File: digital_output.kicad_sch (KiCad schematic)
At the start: 12 parts, among them Q1 AOSP21321, Q2 AOSP21321, Q3 NMOS, Q4 NMOS

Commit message: more routing
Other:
- moved on the sheet: Q4
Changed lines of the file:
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@@
+	)
+	(junction
+		(at 72.39 67.31)
+		(diameter 0)
+		(color 0 0 0 0)
 	)
 	(junction
@@
 		(color 0 0 0 0)
 	)
-	(junction
-		(at 71.12 67.31)
-		(diameter 0)
-		(color 0 0 0 0)
-	)
 	(wire
 		(pts
@@
 	(wire
 		(pts
+			(xy 63.5 88.9) (xy 62.23 88.9)
+		)
+		(stroke
+			(width 0)
+			(type default)
+		)
+	)
+	(wire
+		(pts
 			(xy 36.83 58.42) (xy 36.83 57.15)
 		)
@@
 	(wire
 		(pts
+			(xy 72.39 67.31) (xy 71.12 67.31)
+		)
+		(stroke
+			(width 0)
+			(type default)
+		)
+	)
+	(wire
+		(pts
+			(xy 63.5 91.44) (xy 63.5 88.9)
+		)
+		(stroke
+			(width 0)
+			(type default)
+		)
+	)
+	(wire
+		(pts
 			(xy 19.05 83.82) (xy 19.05 88.9)
 		)
@@
 	(wire
 		(pts
-			(xy 71.12 67.31) (xy 71.12 83.82)
+			(xy 72.39 67.31) (xy 72.39 86.36)
 		)
 		(stroke
@@
 	(wire
 		(pts
+			(xy 71.12 95.25) (xy 71.12 99.06)
+		)
+		(stroke
+			(width 0)
+			(type default)
+		)
+	)
+	(wire
+		(pts
 			(xy 53.34 83.82) (xy 53.34 88.9)
 		)
@@
 	(wire
 		(pts
-			(xy 71.12 93.98) (xy 71.12 99.06)
+			(xy 72.39 96.52) (xy 72.39 95.25)
 		)
 		(stroke
@@
 	(wire
 		(pts
-			(xy 71.12 67.31) (xy 72.39 67.31)
-		)
-		(stroke
-			(width 0)
-			(type default)
-		)
-	)
-	(wire
-		(pts
 			(xy 53.34 90.17) (xy 53.34 88.9)
 		)
@@
 	(wire
 		(pts
-			(xy 62.23 88.9) (xy 63.5 88.9)
+			(xy 63.5 91.44) (xy 64.77 91.44)
 		)
 		(stroke
@@
 		(pts
 			(xy 27.94 88.9) (xy 29.21 88.9)
+		)
+		(stroke
+			(width 0)
+			(type default)
+		)
+	)
+	(wire
+		(pts
+			(xy 72.39 95.25) (xy 71.12 95.25)
 		)
 		(stroke
@@
 	(symbol
 		(lib_id "Simulation_SPICE:NMOS")
-		(at 68.58 88.9 0)
+		(at 69.85 91.44 0)
 		(unit 1)
 		(exclude_from_sim no)
@@
 		(dnp no)
 		(property "Reference" "Q4"
-			(at 63.5 91.44 0)
+			(at 64.77 93.98 0)
 			(effects
 				(font
@@
 		)
 		(property "Value" "NMOS"
-			(at 63.5 93.98 0)
+			(at 64.77 96.52 0)
 			(effects
 				(font
@@
 		)
 		(property "Footprint" "Package_TO_SOT_SMD:SOT-23"
-			(at 73.66 86.36 0)
+			(at 74.93 88.9 0)
 			(effects
 				(font
@@
 		)
 		(property "Datasheet" "https://ngspice.sourceforge.io/docs/ngspice-manual.pdf"
-			(at 68.58 101.6 0)
+			(at 69.85 104.14 0)
 			(effects
 				(font
@@
 		)
 		(property "Description" ""
-			(at 68.58 88.9 0)
+			(at 69.85 91.44 0)
 			(effects
 				(font
@@
 		)
 		(property "Sim.Device" "NMOS"
-			(at 68.58 106.045 0)
+			(at 69.85 108.585 0)
 			(effects
 				(font
@@
 		)
 		(property "Sim.Type" "VDMOS"
-			(at 68.58 107.95 0)
+			(at 69.85 110.49 0)
 			(effects
 				(font
@@
 		)
 		(property "Sim.Pins" "1=D 2=G 3=S"
-			(at 68.58 104.14 0)
+			(at 69.85 106.68 0)
 			(effects
 				(font
@@
 		)
 		(property "LCSC#" "C20917"
-			(at 68.58 88.9 0)
+			(at 69.85 91.44 0)
 			(effects
 				(font
@@
 		)
 		(property "Manufacturer" "Alpha & Omega Semicon"
-			(at 68.58 88.9 0)
+			(at 69.85 91.44 0)
 			(effects
 				(font
@@
 		)
 		(property "Part#" "AO3400A"
-			(at 68.58 88.9 0)
-			(effects
-				(font
+			(at 69.85 91.44 0)
+			(effects
+				(font

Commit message: added comment for mosfet todo
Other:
- note added: "@TODO: fix mosfet rotation issue!!!"
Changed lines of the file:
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@@
+		)
+	)
+	(text "@TODO:\nfix mosfet rotation issue!!!"
+		(exclude_from_sim no)
+		(at 40.64 109.22 0)
+		(effects
+			(font
+				(size 1.27 1.27)
+			)
+			(justify left)
 		)
 	)

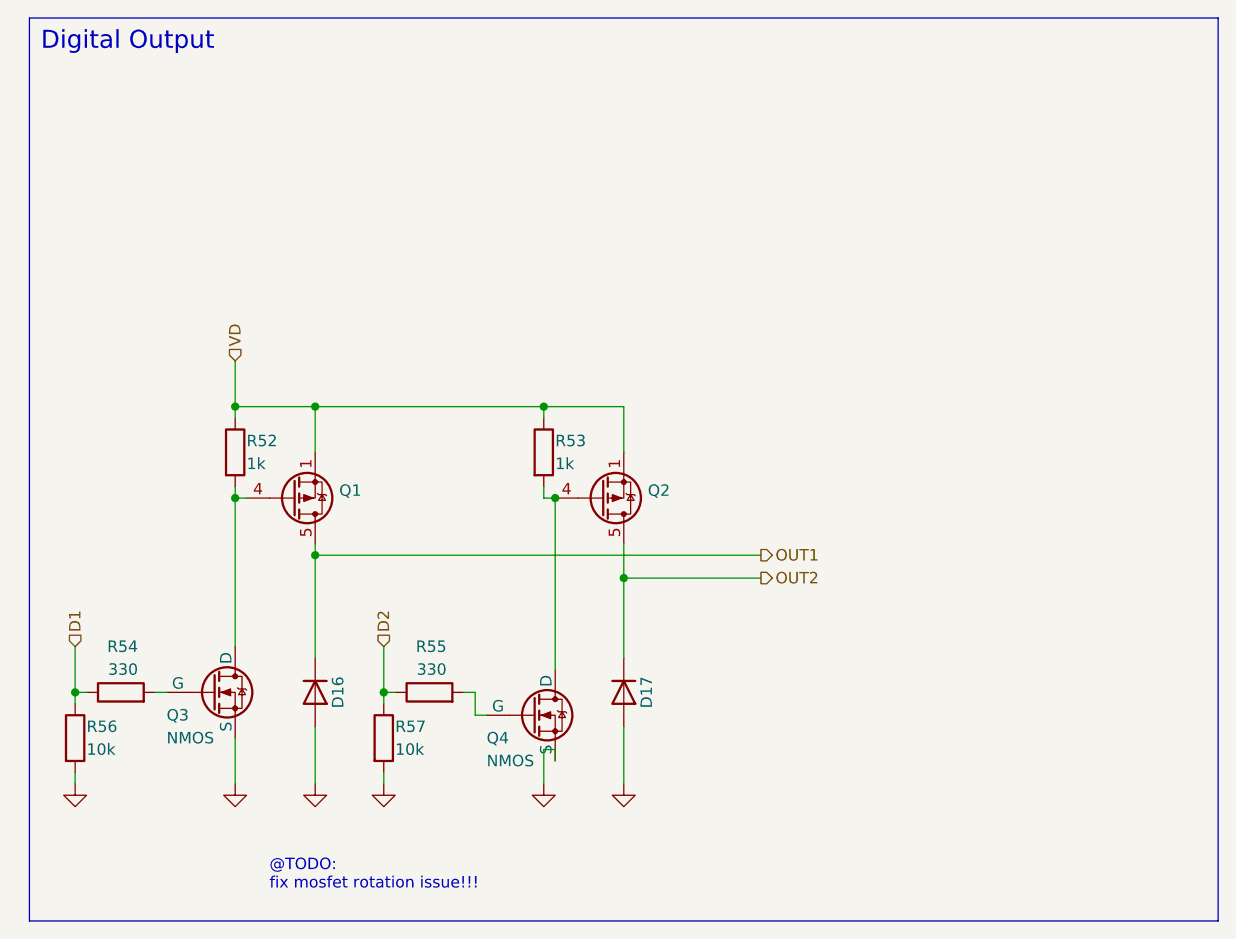
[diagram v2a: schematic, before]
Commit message: fixed transistor rotation issue, filter vs farrite bead, 5V supply for servos, and others in scematic
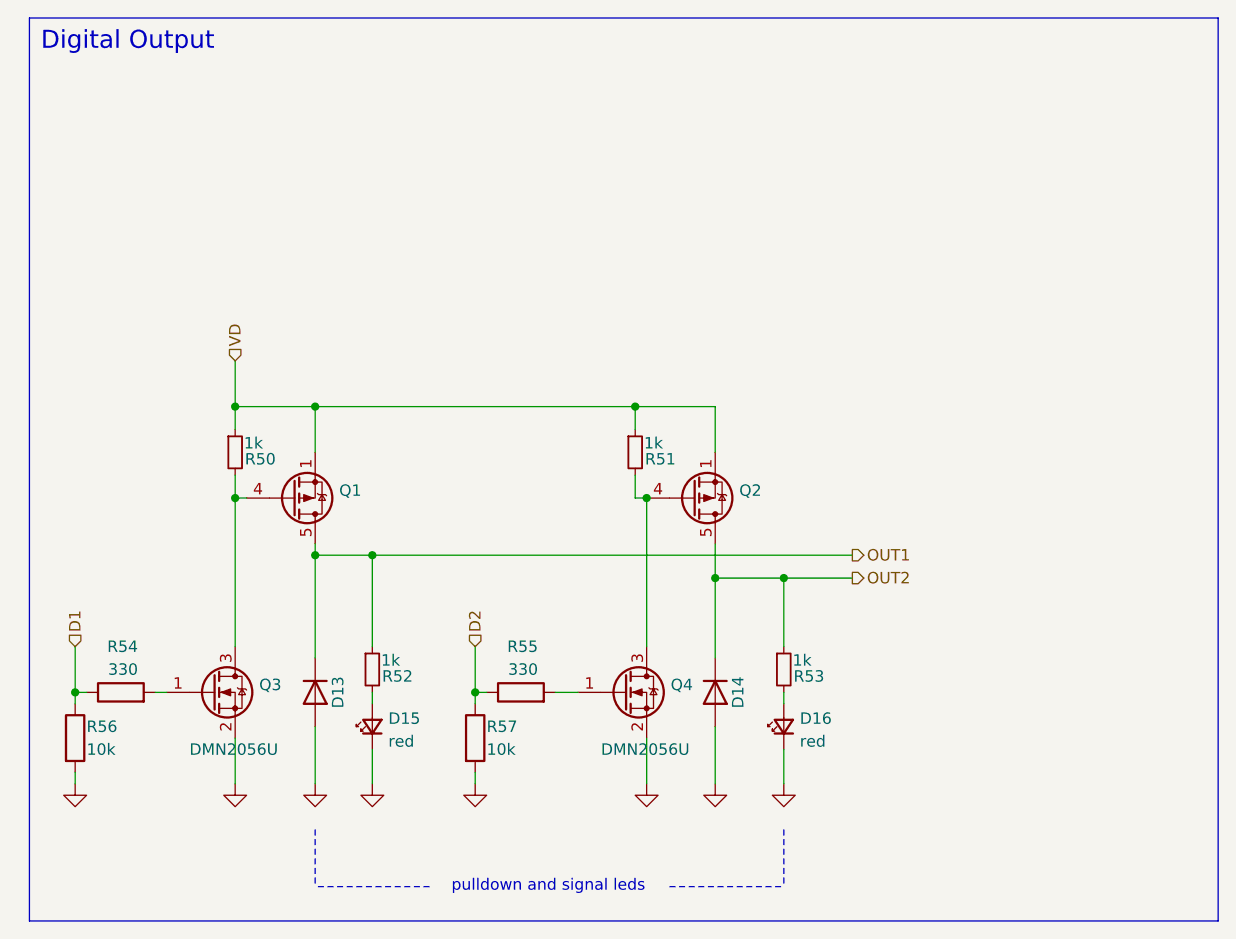
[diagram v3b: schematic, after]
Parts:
- removed Q3, Q4: NMOS, Package_TO_SOT_SMD:SOT-23, symbol Simulation_SPICE:NMOS
- removed R52, R53: 1k, Resistor_SMD:R_0603_1608Metric_Pad0.98x0.95mm_HandSolder, symbol Device:R
- added D15, D16: red, LED_SMD:LED_0603_1608Metric, symbol Device:LED_Small
- added Q3, Q4: DMN2056U, Package_TO_SOT_SMD:SOT-23, symbol Transistor_FET:DMG2302U
- added R50, R51, R52, R53: 1k, Resistor_SMD:R_0402_1005Metric, symbol Device:R_Small
- renumbered D16 to D13, D17 to D14
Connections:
- net GND: now also D15.1 (K), D16.1 (K), Q3.2 (S), Q4.2 (S)
- net OUT1: now also R52.1
- net OUT2: now also R53.1
- net VD: now also R50.1, R51.1
- net at Q1.4 (G): now also Q3.3 (D), R50.2
- net at Q2.4 (G): now also Q4.3 (D), R51.2
- net at R55.2: now also Q4.1 (G)
- net at R54.2: now also Q3.1 (G)
- new net: D15.2 (A), R52.2
- new net: D16.2 (A), R53.2
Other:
- note added: "pulldown and signal leds"
- note removed: "@TODO: fix mosfet rotation issue!!!"
- moved on the sheet: D14, Q2, R55, R57

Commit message: started routing
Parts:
- D13, D14: footprint Diode_SMD:D_SOD-323_HandSoldering -> Diode_SMD:D_SOD-123F; LCSC (none) -> C64898; LCSC# C7528872 -> (none)
- D15, D16: LCSC (none) -> C965799; LCSC# C965799 -> (none)
- Q1, Q2: footprint Package_SO:SO-8_3.9x4.9mm_P1.27mm -> Package_SO:SOIC-8_3.9x4.9mm_P1.27mm; LCSC (none) -> C560863; LCSC# C560863 -> (none)
- R52: renamed from R50; LCSC (none) -> C11702; LCSC# C2906899 -> (none); Manufacturer FOJAN -> (none); Part# FRC0402J102 TS -> (none)
- R53: renamed from R51; LCSC (none) -> C11702; LCSC# C2906899 -> (none); Manufacturer FOJAN -> (none); Part# FRC0402J102 TS -> (none)
- R54: renamed from R52; LCSC (none) -> C11702; LCSC# C2906899 -> (none); Manufacturer FOJAN -> (none); Part# FRC0402J102 TS -> (none)
- R55: renamed from R53; LCSC (none) -> C11702; LCSC# C2906899 -> (none); Manufacturer FOJAN -> (none); Part# FRC0402J102 TS -> (none)
- R56: renamed from R54; footprint Resistor_SMD:R_0603_1608Metric_Pad0.98x0.95mm_HandSolder -> Resistor_SMD:R_0402_1005Metric; LCSC (none) -> C25104; LCSC# C23138 -> (none)
- R57: renamed from R55; footprint Resistor_SMD:R_0603_1608Metric_Pad0.98x0.95mm_HandSolder -> Resistor_SMD:R_0402_1005Metric; LCSC (none) -> C25104; LCSC# C23138 -> (none)
- R58: renamed from R56; footprint Resistor_SMD:R_0603_1608Metric_Pad0.98x0.95mm_HandSolder -> Resistor_SMD:R_0402_1005Metric; LCSC (none) -> C25744; LCSC# C25804 -> (none)
- R59: renamed from R57; footprint Resistor_SMD:R_0603_1608Metric_Pad0.98x0.95mm_HandSolder -> Resistor_SMD:R_0402_1005Metric; LCSC (none) -> C25744; LCSC# C25804 -> (none)
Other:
- note added: "use 0402!!"
- moved on the sheet: D13, D14, D15, D16, Q1, Q2, Q3, Q4, R52, R53, R54, R55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

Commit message: finished routing
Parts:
- added R32, R73: 10k, Resistor_SMD:R_0402_1005Metric, symbol Device:R
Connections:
- net GND: now also R32.2, R73.2
- net OUT1: now also R32.1
- net OUT2: now also R73.1
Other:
- note removed: "use 0402!!"
- moved on the sheet: D14, D16, Q2, Q4, R53, R55, R57, R59

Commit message: started silkscrean
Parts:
- renumbered D14 to D10, D15 to D11, D16 to D12, D13 to D9, R52 to R49, R53 to R50, R54 to R51, R55 to R52, R32 to R53, R73 to R54, R56 to R55, R57 to R56, R58 to R57, R59 to R58

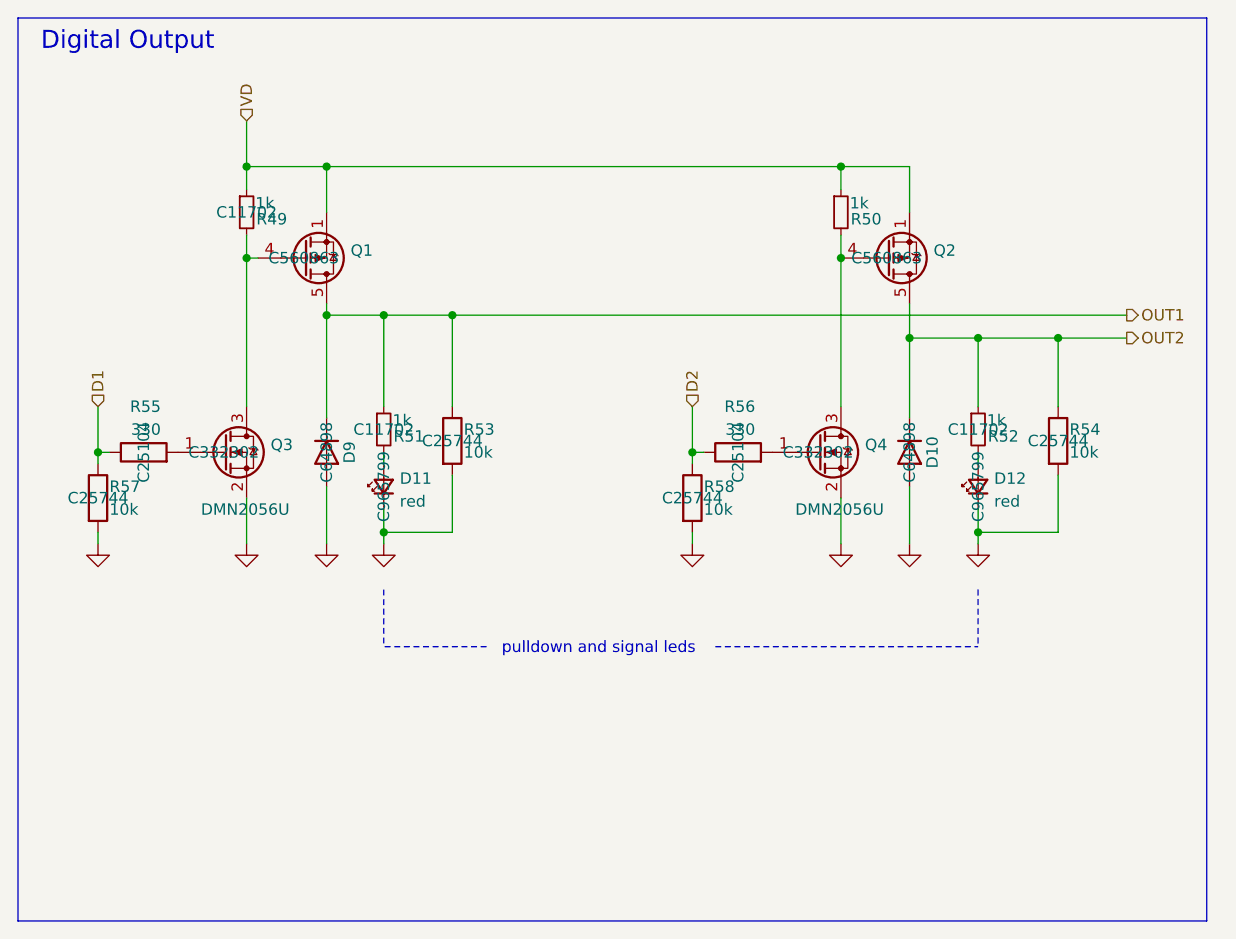
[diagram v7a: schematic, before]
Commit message: high current inputs: change pmos pullup and led resistors
Apparently Kicad also saved files in a new format.
I was using Kicad version 10.0
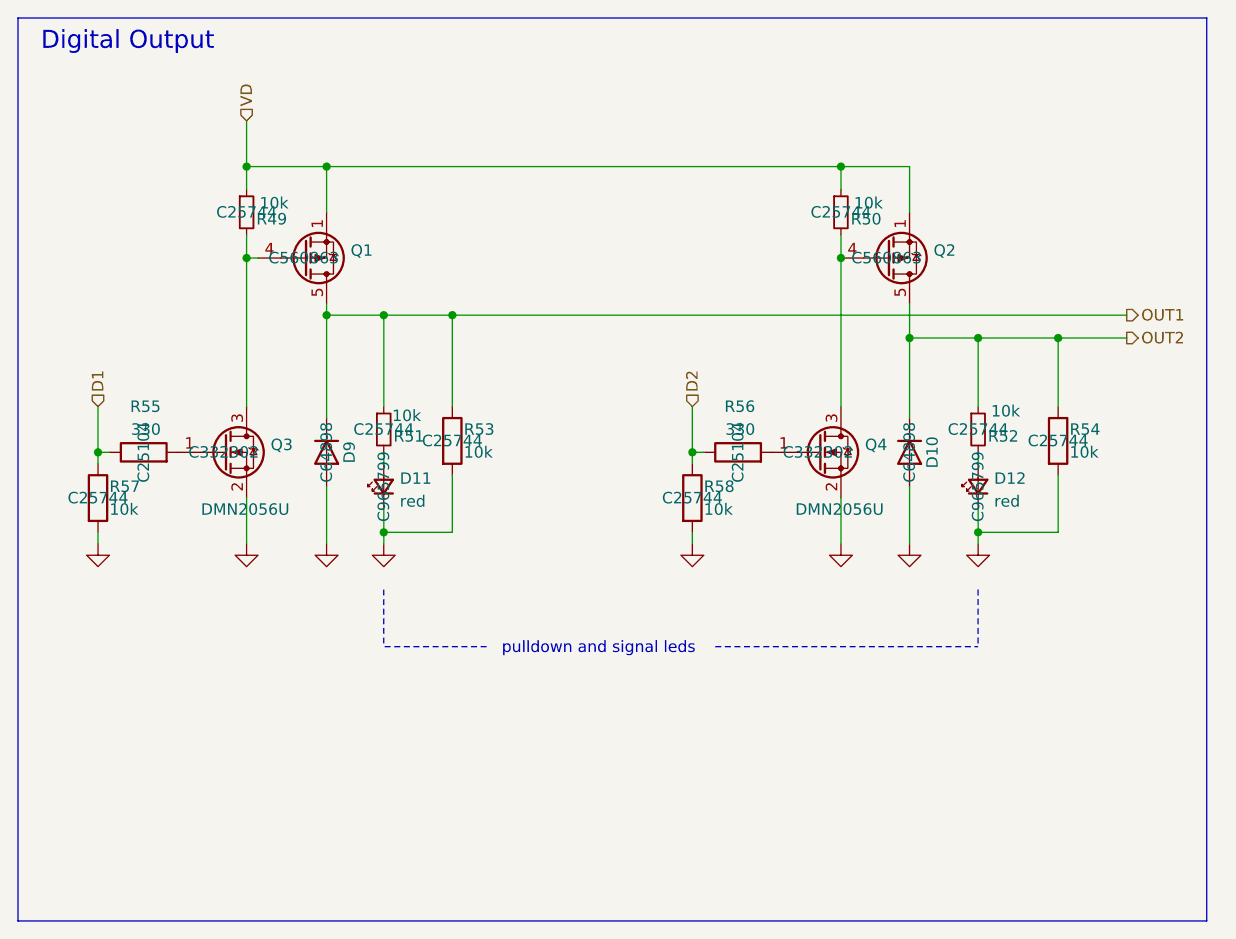
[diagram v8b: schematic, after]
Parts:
- R49, R50, R51, R52: value 1k -> 10k; LCSC C11702 -> C25744
